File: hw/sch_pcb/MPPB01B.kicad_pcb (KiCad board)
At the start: 2 copper layers, 101.1 x 101.1 mm, 27 parts, among them P1 BTH-030-01-F-D-A, P10 SATA7-67491-1030, P11 HEADER_2x05_PARALLEL, P2 BTH-030-01-F-D-A, P3 BTH-030-01-F-D-A, P4 BTH-030-01-F-D-A, P5 SAS_mini_1888174-6, P6 SAS_mini_1888174-6, P7 HEADER_2x13, P9 HEADER_2x03_PARALLEL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

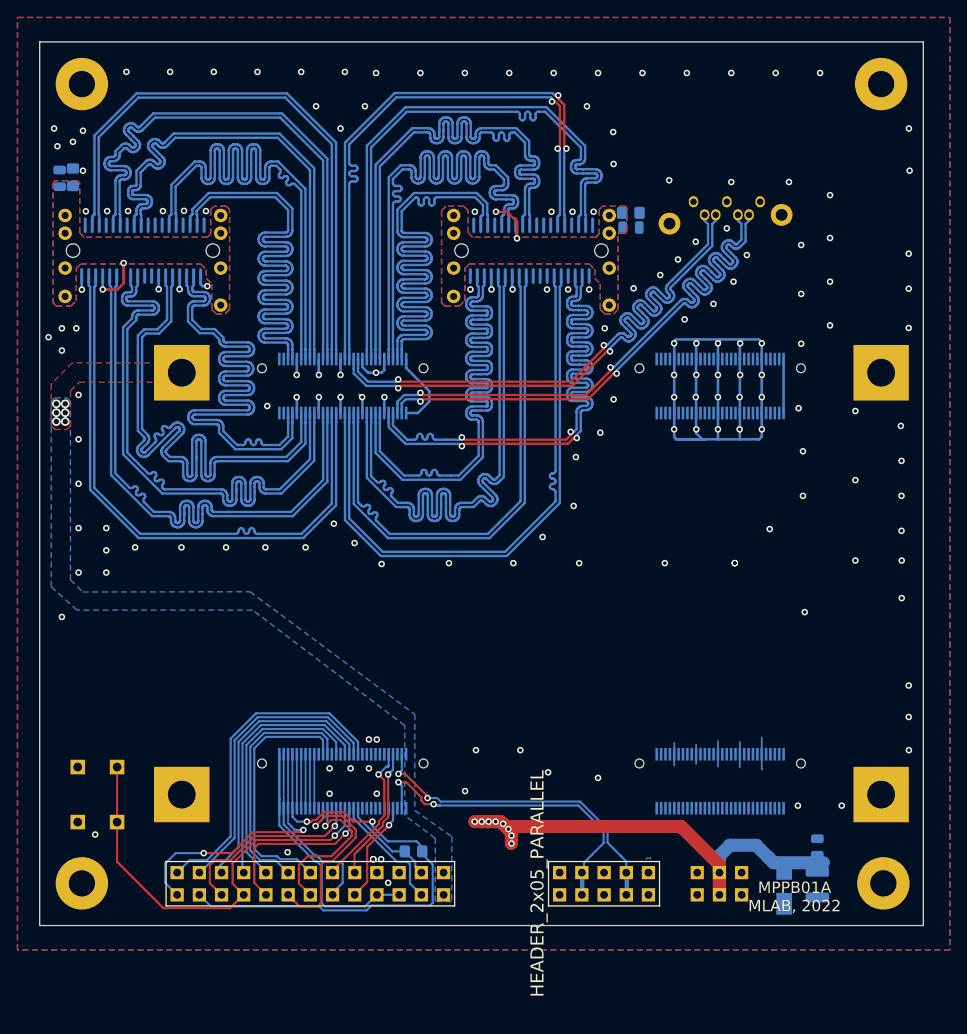
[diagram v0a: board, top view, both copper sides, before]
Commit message: Routovani cesticek, uprava pinoutu
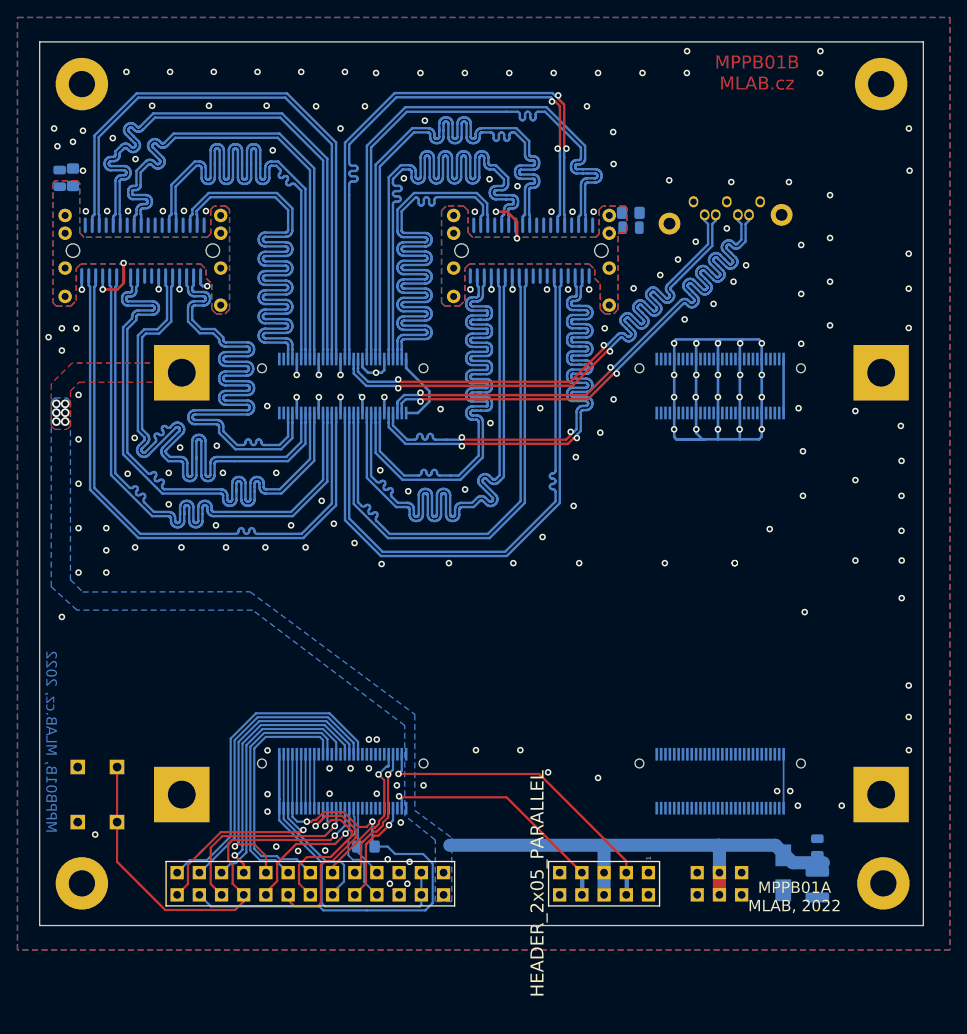
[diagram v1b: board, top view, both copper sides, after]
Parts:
- moved R3 5.48 mm to (144.2, 183.8)
- moved D1 1.55 mm to (192.0, 186.8)
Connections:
- P11 pad 5: /POWER/SYS-5POV -> /SYS-5POV
- P11 pad 6: /POWER/SYS-5POV -> /SYS-5POV
- P7 pad 1: /POWER/SYS-5POV -> /SYS-5POV
- P7 pad 17: /VADC_N -> /SPDIF
- P7 pad 2: /POWER/SYS-5POV -> /SYS-5POV
- P7 pad 21: /SPDIF -> /VADC_N
- P7 pad 3: /UART_RX -> /3P3V
- P7 pad 4: /UART_TX -> /3P3V
- P7 pad 6: /3P3V -> GND
- P7 pad 7: GND -> /UART_RX
- P7 pad 8: /3P3V -> /UART_TX
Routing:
- net GND: track 146.0 -> 131.7 mm, vias 176 -> 212
- net /I2C_SDA: track 37.8 -> 28.6 mm, vias 2 -> 1
- net /SOUTH/VDDIO: track 0.00 -> 6.17 mm
- net /3P3V: track 28.7 -> 34.1 mm
- net /SYS-5POV: track 51.0 -> 55.2 mm, vias 14 -> 6
- net /USER_LED: track 20.2 -> 16.6 mm
- net /UART_RX: track 11.2 -> 8.26 mm
- net /RESET_N: track 49.0 -> 51.7 mm
- net /VDD_GPIO: track 31.6 -> 28.9 mm, vias 2 -> 1
- net /SPDIF: track 31.8 -> 34.3 mm, vias 0 -> 1
- net /UART_TX: track 13.8 -> 12.1 mm
- net /JTAG_BOOT_EN: track 29.4 -> 31.0 mm, vias 0 -> 1
- net /VDD_ADJ: track 59.4 -> 60.7 mm
- net /I2C_SCL: track 37.6 -> 36.5 mm, vias 2 -> 1
- net /VADC_P: track 21.9 -> 22.9 mm
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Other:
- board text added: "1 SYS_5V 3 3.3 V 5 GND 7 RX 9 REG_EN3 11 PROG_IO 13 JTAG_TCK 15 JTAG_TMS 17 VADC_N 19 JTAG_BOOT_EN 21 SPDIF 23 TURBO_MODE 25 DSP_FLAG"
- board text added: "5"
- board text added: "GND 5V GND"
- board text added: "GND SCL 5V SDA GND"
- board text added: "MPPB01B MLAB.cz"
- board text added: "MPPB01B, MLAB.cz, 2022"
- board text added: "Mechanical Parallella peripheral board"
- board text added: "Peripheral"
- board text added: "Peripheral pinout"
- board text added: "SYS 5V 2 3.3V 4 GND 6 TX 8 REG_EN4 10 2.5V 12 JTAG_TDI 14 JTAG_TDO 16 USER_LED 18 RESET_N 20 VADC_P 22 VDD_ADJ 24 VDD_GPIO 26"
- board text added: "www.mlab.cz 2022"
- board text removed: "1 SYS_5V 3 RX 5 GND 7 GND 9 REG_EN3 11 PROG_IO 13 JTAG_TCK 15 JTAG_TMS 17 VADC_N 19 JTAG_BOOT_EN 21 VADC_N 23 TURBO_MODE 25 DSP_FLAG"
- board text removed: "GND"
- board text removed: "I2C_SCL"
- board text removed: "I2C_SDA"
- board text removed: "P7"
- board text removed: "P7 Pinout"
- board text removed: "SYS 5V 2 TX 4 3p3V 6 3p3V 8 REG_EN4 10 2p5V 12 JTAG_TDI 14 JTAG_TDO 16 USER_LED 18 RESET_N 20 VADC_P 22 VDD_ADJ 24 VDD_GPIO 26"
- board text removed: "UART_RX"
- board text removed: "UART_TX"
- board text removed: "VDD_ADJ"

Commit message: uprava silkscreenu
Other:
- board text added: "1 SYS_5V 3 3.3 V 5 GND 7 RX 9 REG_EN3 11 PROG_IO 13 JTAG_TCK 15 JTAG_TMS 17 SPDIF 19 JTAG_BOOT_EN 21 VADC_N 23 TURBO_MODE 25 DSP_FLAG"
- board text removed: "1 SYS_5V 3 3.3 V 5 GND 7 RX 9 REG_EN3 11 PROG_IO 13 JTAG_TCK 15 JTAG_TMS 17 VADC_N 19 JTAG_BOOT_EN 21 SPDIF 23 TURBO_MODE 25 DSP_FLAG"
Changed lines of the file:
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@@
     (property "Sheetname" "POWER")
     (attr through_hole)
-    (fp_text reference "P7" (at -1 -18.1) (layer "B.SilkS") hide
-      (effects (font (size 1.5 1.5) (thickness 0.15)) (justify mirror))
-    )
-    (fp_text value "HEADER_2x13" (at 0 17.78 90) (layer "B.SilkS")
+    (fp_text reference "P7" (at 3.8 -13.1 180) (layer "B.SilkS")
+      (effects (font (size 1 1) (thickness 0.1)) (justify mirror))
+    )
+    (fp_text value "HEADER_2x13" (at 0 17.78 90) (layer "B.SilkS") hide
       (effects (font (size 1.5 1.5) (thickness 0.15)) (justify mirror))
     )
@@
     (property "Sheetname" "POWER")
     (attr through_hole)
-    (fp_text reference "P11" (at 0 -7.62 90) (layer "F.SilkS") hide
-      (effects (font (size 1.5 1.5) (thickness 0.15)))
-    )
-    (fp_text value "HEADER_2x05_PARALLEL" (at 0 7.62 90) (layer "F.SilkS")
-      (effects (font (size 1.5 1.5) (thickness 0.15)))
-    )
-    (fp_text user "1" (at -2.921 -5.08 90) (layer "F.SilkS")
-      (effects (font (size 0.5 0.5) (thickness 0.05)))
+    (fp_text reference "P11" (at 3.8 -4.8 180) (layer "B.SilkS")
+      (effects (font (size 1 1) (thickness 0.1)) (justify mirror))
+    )
+    (fp_text value "HEADER_2x05_PARALLEL" (at 0 7.62 90) (layer "B.SilkS") hide
+      (effects (font (size 1.5 1.5) (thickness 0.15)) (justify mirror))
+    )
+    (fp_text user "1" (at -2.921 -5.08 90) (layer "B.SilkS") hide
+      (effects (font (size 0.5 0.5) (thickness 0.05)) (justify mirror))
     )
     (fp_line (start 2.54 -6.35) (end 2.54 6.35) (layer "F.SilkS") (width 0.15))
@@
     (property "Sheetname" "")
     (attr smd)
-    (fp_text reference "P5" (at 4 6.29) (layer "B.SilkS")
-      (effects (font (size 1 1) (thickness 0.15)) (justify mirror))
+    (fp_text reference "P5" (at 9.005 7.319995) (layer "B.SilkS")
+      (effects (font (size 1 1) (thickness 0.1)) (justify mirror))
     )
     (fp_text value "SAS_mini_1888174-6" (at 2.3 -8.6) (layer "B.Fab")
@@
     (attr through_hole)
     (fp_text reference "P9" (at 3.81 -2.8352) (layer "B.SilkS")
-      (effects (font (size 1 1) (thickness 0.15)) (justify mirror))
+      (effects (font (size 1 1) (thickness 0.1)) (justify mirror))
     )
     (fp_text value "HEADER_2x03_PARALLEL" (at 0 -5.08 -90) (layer "B.SilkS") hide
@@
     (property "exclude_from_bom" "")
     (attr smd exclude_from_bom)
-    (fp_text reference "P6" (at 4 6.29) (layer "B.SilkS")
-      (effects (font (size 1 1) (thickness 0.15)) (justify mirror))
+    (fp_text reference "P6" (at 9.155 7.119995) (layer "B.SilkS")
+      (effects (font (size 1 1) (thickness 0.1)) (justify mirror))
     )
     (fp_text value "SAS_mini_1888174-6" (at 2.3 -8.6) (layer "B.Fab")
@@
     (property "Sheetname" "")
     (attr through_hole)
-    (fp_text reference "P10" (at 2.8956 5.08) (layer "B.SilkS")
-      (effects (font (size 1 1) (thickness 0.2)) (justify mirror))
+    (fp_text reference "P10" (at 3.243 5.318) (layer "B.SilkS")
+      (effects (font (size 1 1) (thickness 0.1)) (justify mirror))
     )
     (fp_text value "SATA7-67491-1030" (at -3.31 3.2) (layer "B.Fab")
@@
   )
   (gr_rect (start 177.85 185.45) (end 165.15 190.55) (layer "B.SilkS") (width 0.15) (fill none))
+  (gr_poly
+    (pts
+      (xy 155.8 187.7)
+      (xy 154.8 186.7)
+      (xy 155.8 185.7)
+    ) (layer "B.SilkS") (width 0.15) (fill solid))
   (gr_line (start 142 102) (end 142 121.5) (layer "B.SilkS") (width 0.15))
   (gr_line (start 206.375 180.975) (end 120.015 180.975) (layer "B.SilkS") (width 0.1))
@@
     (effects (font (size 1 1) (thickness 0.2)) (justify mirror))
   )
-  (gr_text "MPPB01B\n" (at 197.5 98.25) (layer "B.SilkS")
+  (gr_text "MPPB01B\n" (at 197.45 96.75) (layer "B.SilkS")
     (effects (font (size 1.8 1.8) (thickness 0.3)) (justify left mirror))
   )
@@
     (effects (font (size 1 1) (thickness 0.15)) (justify mirror))
   )
-  (gr_text "1  SYS_5V\n3  3.3 V\n5  GND\n7  RX\n9  REG_EN3\n11 PROG_IO\n13 JTAG_TCK\n15 JTAG_TMS\n17 VADC_N\n19 JTAG_BOOT_EN\n21 SPDIF\n23 TURBO_MODE\n25 DSP_FLAG" (at 141.5 112) (layer "B.SilkS")
+  (gr_text "1  SYS_5V\n3  3.3 V\n5  GND\n7  RX\n9  REG_EN3\n11 PROG_IO\n13 JTAG_TCK\n15 JTAG_TMS\n17 SPDIF\n19 JTAG_BOOT_EN\n21 VADC_N\n23 TURBO_MODE\n25 DSP_FLAG" (at 141.5 112) (layer "B.SilkS")
     (effects (font (size 0.9 0.9) (thickness 0.15)) (justify left mirror))
   )
@@
     (effects (font (size 0.9 0.9) (thickness 0.15)) (justify right mirror))
   )
-  (gr_text "SYNC" (at 185.5 115.75) (layer "B.SilkS")
+  (gr_text "SYNC" (at 185.6 107.2) (layer "B.SilkS")
     (effects (font (size 1.5 1.5) (thickness 0.3)) (justify mirror))
   )
@@
     (effects (font (size 1 1) (thickness 0.15)) (justify mirror))
   )
-  (gr_text "Peripheral\n" (at 152.25 182.75) (layer "B.SilkS")
+  (gr_text "Peripheral\n" (at 152.8 182.75) (layer "B.SilkS")
     (effects (font (size 1.5 1.5) (thickness 0.3)) (justify mirror))
   )
@@
     (effects (font (size 1.3 1.3) (thickness 0.2)) (justify mirror))
   )
-  (gr_text "www.mlab.cz\n2022" (at 197.25 104) (layer "B.SilkS")
+  (gr_text "www.mlab.cz\n2022" (at 197.2 102.5) (layer "B.SilkS")
     (effects (font (size 1 1) (thickness 0.15)) (justify left mirror))
   )
-  (gr_text "Mechanical Parallella peripheral board" (at 182.5 101) (layer "B.SilkS")
+  (gr_text "Mechanical Parallella peripheral board" (at 182.45 99.5) (layer "B.SilkS")
     (effects (font (size 1 1) (thickness 0.15)) (justify mirror))
   )
@@
   (via (at 205.454 135.626) (size 0.75) (drill 0.4) (layers "F.Cu" "B.Cu") (net 4))
   (via (at 206.454 106.426) (size 0.75) (drill 0.4) (layers "F.Cu" "B.Cu") (net 4))
-  (via (at 186.054 107.726) (size 0.75) (drill 0.4) (layers "F.Cu" "B.Cu") (net 4))
+  (via (at 185.6 108.5) (size 0.75) (drill 0.4) (layers "F.Cu" "B.Cu") (net 4))
   (via (at 178.954 107.526) (size 0.75) (drill 0.4) (layers "F.Cu" "B.Cu") (net 4))
   (via (at 194.054 126.226) (size 0.75) (drill 0.4) (layers "F.Cu" "B.Cu") (net 4))
-  (via (at 194.054 114.926) (size 0.75) (drill 0.4) (layers "F.Cu" "B.Cu") (net 4))
+  (via (at 194.7 115) (size 0.75) (drill 0.4) (layers "F.Cu" "B.Cu") (net 4))
   (via (at 192.654 107.726) (size 0.75) (drill 0.4) (layers "F.Cu" "B.Cu") (net 4))
   (via (at 197.354 114.126) (size 0.75) (drill 0.4) (layers "F.Cu" "B.Cu") (net 4))
@@
   (via (at 168.275 139.192) (size 0.75) (drill 0.4) (layers "F.Cu" "B.Cu") (net 4))
   (via (at 117 141.1) (size 0.75) (drill 0.4) (layers "F.Cu" "B.Cu") (free) (net 4))
-  (via (at 171.577 124.46) (size 0.75) (drill 0.4) (layers "F.Cu" "B.Cu") (net 4))
+  (via (at 171.5 125.2) (size 0.75) (drill 0.4) (layers "F.Cu" "B.Cu") (net 4))
   (via (at 184.531 126.1745) (size 0.75) (drill 0.4) (layers "F.Cu" "B.Cu") (net 4))
   (via (at 111.887 101.854) (size 0.75) (drill 0.4) (layers "F.Cu" "B.Cu") (net 4))

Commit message: Minor improvements in silksceen layout.
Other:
- board text added: "MPPB01B MLAB, 2022"
- board text removed: "MPPB01A MLAB, 2022"
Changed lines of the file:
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@@
       (effects (font (size 1.5 1.5) (thickness 0.15)) (justify mirror))
-    )
-    (fp_text user "1" (at -2.921 2.54 -90) (layer "B.SilkS")
-      (effects (font (size 0.5 0.5) (thickness 0.05)) (justify mirror))
     )
     (fp_text user "${REFERENCE}" (at 0.127 0.254 180) (layer "B.Fab")
@@
     (property "Sheetname" "")
     (attr smd)
-    (fp_text reference "D1" (at 0 1.44) (layer "B.SilkS")
+    (fp_text reference "D1" (at 0 -0.024) (layer "B.SilkS")
       (effects (font (size 1 1) (thickness 0.15)) (justify mirror))
     )
@@
     (property "Sheetname" "")
     (attr smd)
-    (fp_text reference "C4" (at 0 1.68 90) (layer "B.SilkS")
+    (fp_text reference "C4" (at -3.163 0.254 90) (layer "B.SilkS")
       (effects (font (size 1 1) (thickness 0.15)) (justify mirror))
     )
@@
     (property "Sheetname" "")
     (attr smd)
-    (fp_text reference "R2" (at 0 1.65 90) (layer "B.SilkS")
+    (fp_text reference "R2" (at -3.036 0 90) (layer "B.SilkS")
       (effects (font (size 1 1) (thickness 0.15)) (justify mirror))
     )
@@
     (effects (font (size 1 1) (thickness 0.15)) (justify mirror))
   )
-  (gr_text "MPPB01A\nMLAB, 2022" (at 193.3 189.5) (layer "F.SilkS")
+  (gr_text "MPPB01B\nMLAB, 2022" (at 160.782 152.908) (layer "F.SilkS")
     (effects (font (size 1.3 1.3) (thickness 0.15)))
   )

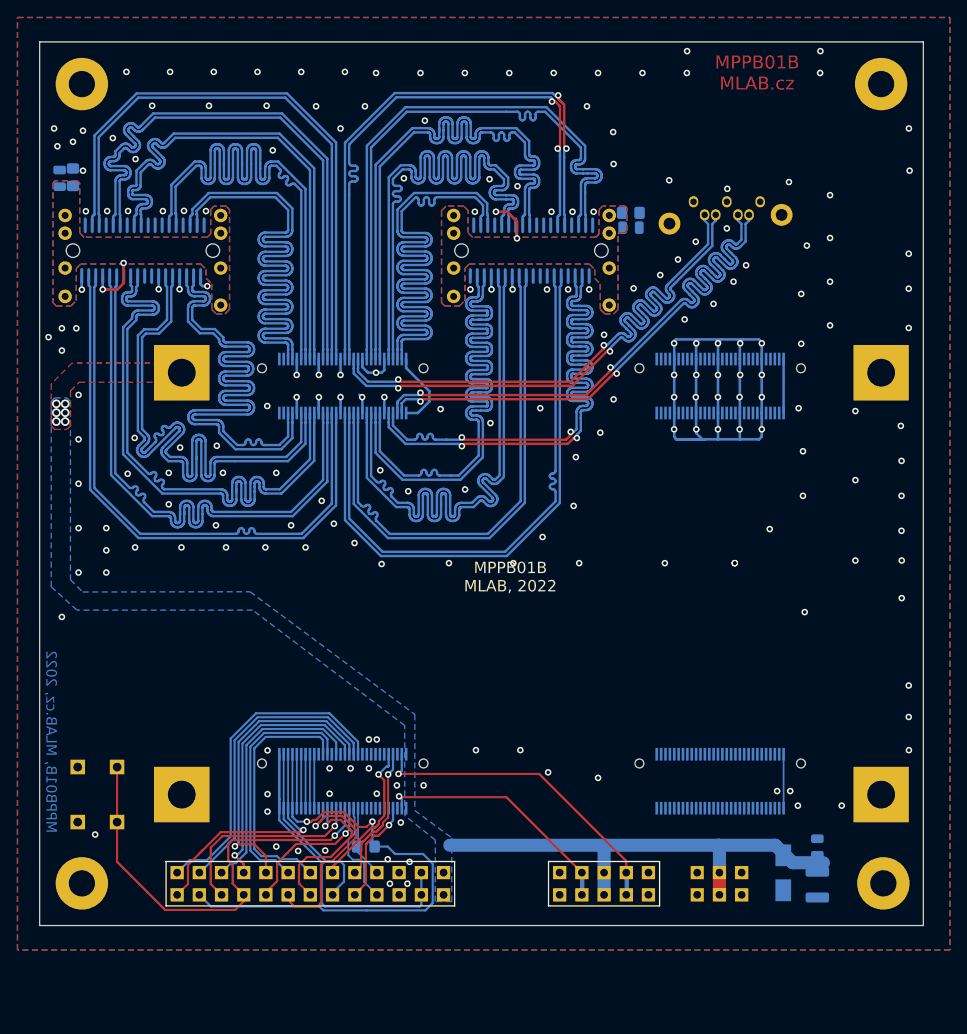
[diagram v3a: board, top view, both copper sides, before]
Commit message: Uprava silksceenu, DRC
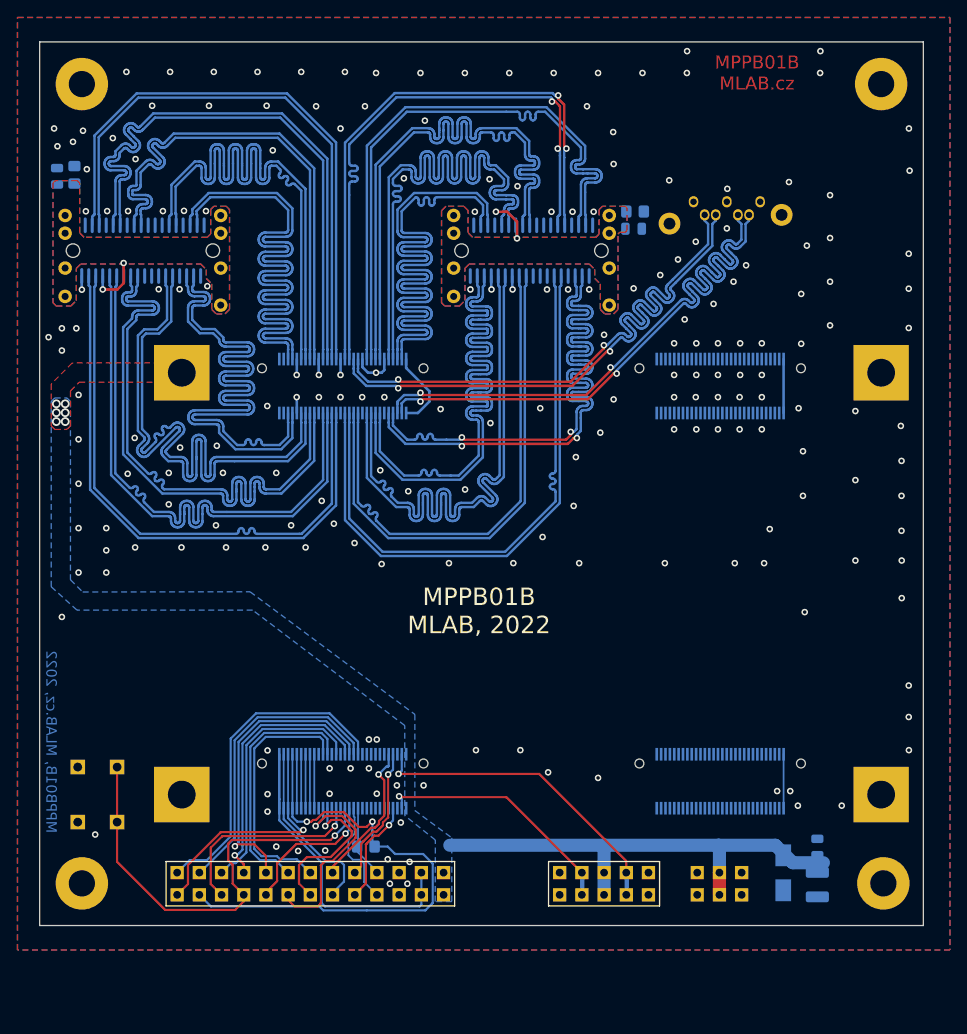
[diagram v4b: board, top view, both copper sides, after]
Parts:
- moved R1 0.51 mm to (175.1, 111.1)
- moved C4 0.38 mm to (108.9, 107.1)
- moved C3 0.32 mm to (174.9, 113.1)
- moved R2 0.32 mm to (110.9, 106.9)
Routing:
- net GND: track 131.7 -> 36.4 mm
- net /JTAG_BOOT_EN: track 31.0 -> 30.3 mm
- net /VDD_GPIO: track 28.9 -> 28.4 mm
